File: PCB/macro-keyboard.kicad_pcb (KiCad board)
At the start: 2 copper layers, 77.6 x 43 mm, 38 parts, among them SW1 SW_Push, SW2 SW_Push, SW3 SW_Push, SW4 SW_Push, SW5 SW_Push, SW6 SW_Push, SW7 SW_Push, SW8 SW_Push, U1 PRTR5V0U2X, U2 ATmega32U4-A, Y1 Crystal_GND24_Small

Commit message: Add gerber files
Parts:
- moved REF** 0.08 mm to (165.9, 83.3)
- moved REF** 0.08 mm to (126.9, 83.4)
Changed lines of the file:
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@@
 			(disableapertmacros no)
 			(usegerberextensions no)
-			(usegerberattributes yes)
-			(usegerberadvancedattributes yes)
-			(creategerberjobfile yes)
+			(usegerberattributes no)
+			(usegerberadvancedattributes no)
+			(creategerberjobfile no)
 			(dashed_line_dash_ratio 12.000000)
 			(dashed_line_gap_ratio 3.000000)
 			(svgprecision 4)
 			(plotframeref no)
-			(viasonmask no)
+			(viasonmask yes)
 			(mode 1)
 			(useauxorigin no)
@@
 			(outputformat 1)
 			(mirror no)
-			(drillshape 1)
+			(drillshape 0)
 			(scaleselection 1)
-			(outputdirectory "")
+			(outputdirectory "Fabrication/")
 		)
 	)
@@
 	(footprint "MountingHole:MountingHole_2.2mm_M2_DIN965"
 		(layer "F.Cu")
-		(at 146.4 109)
+		(at 146.425 108.975)
 		(descr "Mounting Hole 2.2mm, no annular, M2, DIN965")
 		(tags "mounting hole 2.2mm no annular m2 din965")
@@
 	(footprint "MountingHole:MountingHole_2.2mm_M2_DIN965"
 		(layer "F.Cu")
-		(at 165.9 83.4)
+		(at 165.925 83.325)
 		(descr "Mounting Hole 2.2mm, no annular, M2, DIN965")
 		(tags "mounting hole 2.2mm no annular m2 din965")
@@
 	(footprint "MountingHole:MountingHole_2.2mm_M2_DIN965"
 		(layer "F.Cu")
-		(at 126.9 83.3)
+		(at 126.925 83.375)
 		(descr "Mounting Hole 2.2mm, no annular, M2, DIN965")
 		(tags "mounting hole 2.2mm no annular m2 din965")
@@
 	)
 	(segment
+		(start 175.4 95.8)
+		(end 177.2 97.6)
+		(width 0.381)
+		(layer "B.Cu")
+		(net 2)
+	)
+	(segment
 		(start 175.724264 94.024264)
 		(end 176.123044 94.024264)
@@
 	)
 	(segment
-		(start 175.4 95.8)
-		(end 177.319 97.719)
+		(start 179.580062 97.6)
+		(end 179.689421 97.490641)
 		(width 0.381)
 		(layer "B.Cu")
@@
 	)
 	(segment
-		(start 179.461062 97.719)
-		(end 179.689421 97.490641)
+		(start 177.2 97.6)
+		(end 179.580062 97.6)
 		(width 0.381)
 		(layer "B.Cu")
@@
 	)
 	(segment
-		(start 177.319 97.719)
-		(end 179.461062 97.719)
-		(width 0.381)
-		(layer "B.Cu")
-		(net 2)
-	)
-	(segment
 		(start 175.4 94.747308)
 		(end 175.4 95.8)
@@
 	)
 	(segment
-		(start 166.029169 103.177275)
-		(end 165.515454 103.177275)
-		(width 0.381)
-		(layer "B.Cu")
-		(net 4)
-	)
-	(segment
 		(start 142.166377 86.533623)
 		(end 142.433623 86.533623)
@@
 	)
 	(segment
-		(start 166.885786 108.614214)
-		(end 166.820421 108.548849)
-		(width 0.381)
-		(layer "B.Cu")
-		(net 4)
-	)
-	(segment
 		(start 142.113623 79.786377)
 		(end 142.113623 80.463623)
@@
 	)
 	(segment
+		(start 166.820421 103.569474)
+		(end 166.175947 102.925)
+		(width 0.381)
+		(layer "B.Cu")
+		(net 4)
+	)
+	(segment
 		(start 181.156667 97.259107)
 		(end 181.156667 98.957887)
@@
 	)
 	(segment
+		(start 166.175947 99.875947)
+		(end 166.175947 102.925)
+		(width 0.381)
+		(layer "B.Cu")
+		(net 4)
+	)
+	(segment
 		(start 178.030642 92.116666)
 		(end 178.030642 95.369358)
@@
 	)
 	(segment
+		(start 166.820421 108.548849)
+		(end 166.820421 103.569474)
+		(width 0.381)
+		(layer "B.Cu")
+		(net 4)
+	)
+	(segment
 		(start 162.137429 93.9688)
 		(end 160.767246 92.598617)
@@
 	)
 	(segment
-		(start 165.515454 103.177275)
-		(end 164.965856 103.726873)
+		(start 183.156667 96.957887)
+		(end 181.157887 96.957887)
 		(width 0.381)
 		(layer "B.Cu")
@@
 	)
 	(segment
-		(start 166.820421 103.968527)
-		(end 166.175947 103.324053)
+		(start 150.753623 79.753623)
+		(end 149.7 78.7)
 		(width 0.381)
 		(layer "B.Cu")
@@
 	)
 	(segment
-		(start 183.156667 96.957887)
-		(end 181.157887 96.957887)
+		(start 163.166377 105.533623)
+		(end 163.166377 105.666377)
 		(width 0.381)
 		(layer "B.Cu")
@@
 	)
 	(segment
-		(start 150.753623 79.753623)
-		(end 149.7 78.7)
+		(start 171.627736 96.670882)
+		(end 173.592559 98.635705)
 		(width 0.381)
 		(layer "B.Cu")
@@
 	)
 	(segment
-		(start 163.166377 105.533623)
-		(end 163.166377 105.666377)
+		(start 166.175947 102.925)
+		(end 165.767729 102.925)
 		(width 0.381)
 		(layer "B.Cu")
@@
 	)
 	(segment
-		(start 171.627736 96.670882)
-		(end 173.592559 98.635705)
+		(start 162.970882 96.670882)
+		(end 166.175947 99.875947)
 		(width 0.381)
 		(layer "B.Cu")
@@
 	)
 	(segment
+		(start 166.885786 108.614214)
+		(end 166.820421 108.548849)
+		(width 0.381)
+		(layer "B.Cu")
+		(net 4)
+	)
+	(segment
 		(start 140.448123 88.251877)
 		(end 142.166377 86.533623)
@@
 	)
 	(segment
-		(start 166.175947 103.324053)
-		(end 166.175947 99.875947)
+		(start 157.350989 99.750989)
+		(end 156.867246 99.267246)
 		(width 0.381)
 		(layer "B.Cu")
@@
 	)
 	(segment
-		(start 157.350989 99.750989)
-		(end 156.867246 99.267246)
+		(start 165.767729 102.925)
+		(end 164.965856 103.726873)
 		(width 0.381)
 		(layer "B.Cu")
@@
 	)
 	(segment
-		(start 166.820421 108.548849)
-		(end 166.820421 103.968527)
-		(width 0.381)
-		(layer "B.Cu")
-		(net 4)
-	)
-	(segment
 		(start 179.4 99.5)
 		(end 180.614554 99.5)
@@
 	)
 	(segment
-		(start 166.175947 103.324053)
-		(end 166.029169 103.177275)
-		(width 0.381)
-		(layer "B.Cu")
-		(net 4)
-	)
-	(segment
 		(start 150.753623 80.463623)
 		(end 150.753623 76.283623)
@@
 		(width 0.381)
 		(layer "B.Cu")
-		(net 4)
-	)
-	(segment
-		(start 166.175947 99.875947)
-		(end 162.970882 96.670882)
-		(width 0.381)
-		(layer "B.Cu")

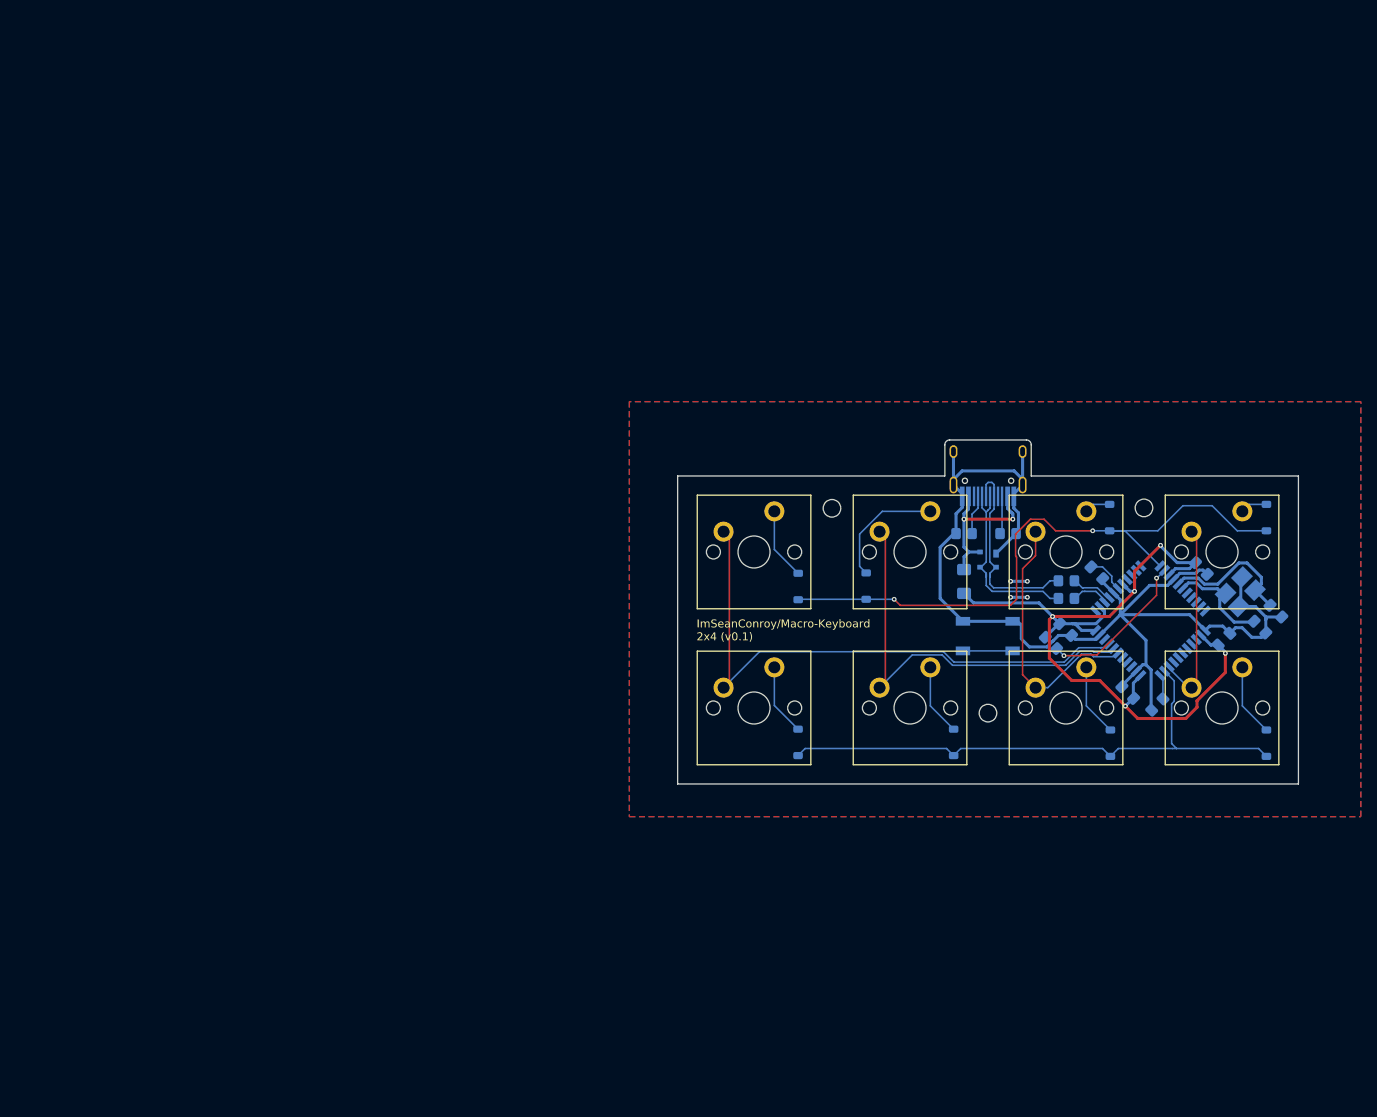
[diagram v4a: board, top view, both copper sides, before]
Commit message: Add boxes to schematic
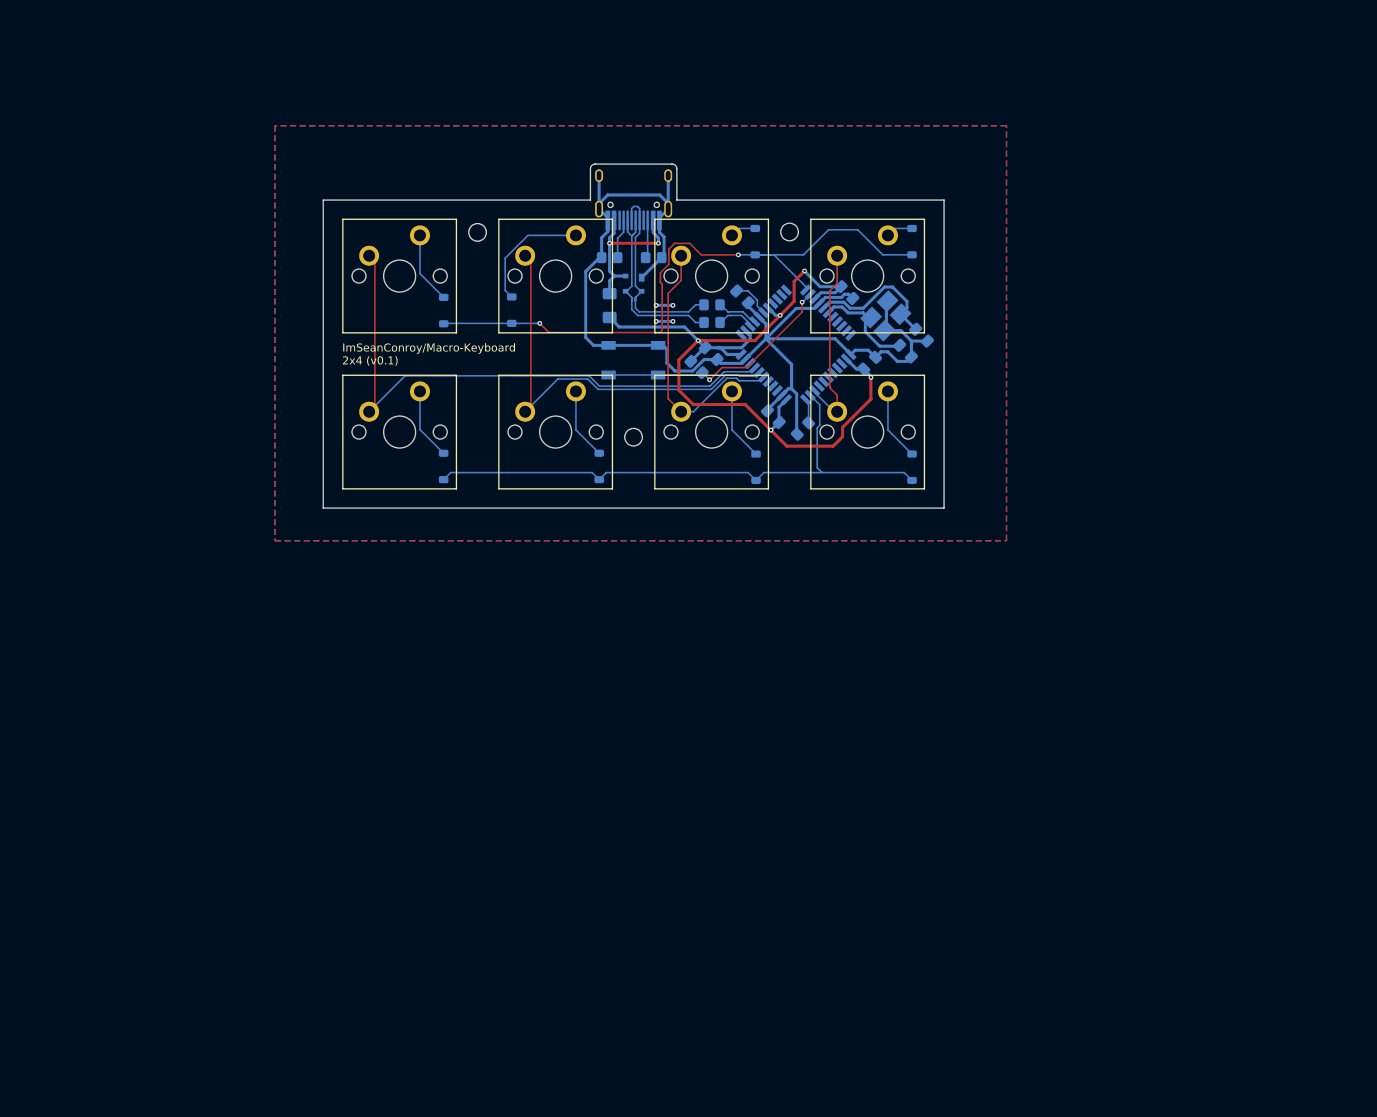
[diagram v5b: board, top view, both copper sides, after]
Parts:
- moved C1 56.1 mm to (136.1, 63.7)
- moved C2 56.1 mm to (138.1, 61.7)
- moved C3 56.1 mm to (131.6, 65.2)
- moved C5 56.1 mm to (119.6, 71.9)
- moved C8 56.1 mm to (115.7, 56.9)
- moved F1 56.1 mm to (99.1, 58.0)
- moved R1 56.1 mm to (104.6, 52.0)
- moved R2 56.1 mm to (99.1, 52.0)
- moved R5 56.1 mm to (110.0, 65.7)
- moved REF** 56.1 mm to (102.1, 74.5)
- moved REF** 56.1 mm to (121.6, 48.8)
- moved SW13 56.1 mm to (102.1, 64.9)
- moved SW2 56.1 mm to (92.4, 54.3)
- moved SW3 56.1 mm to (111.9, 54.3)
- moved SW4 56.1 mm to (131.4, 54.3)
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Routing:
- net +5V: track 100.9 -> 104.9 mm
- net col3: track 24.0 -> 26.1 mm
- net row0: track 79.6 -> 80.9 mm
- net GND: track 147.0 -> 148.0 mm
- net RESET: track 31.4 -> 30.8 mm

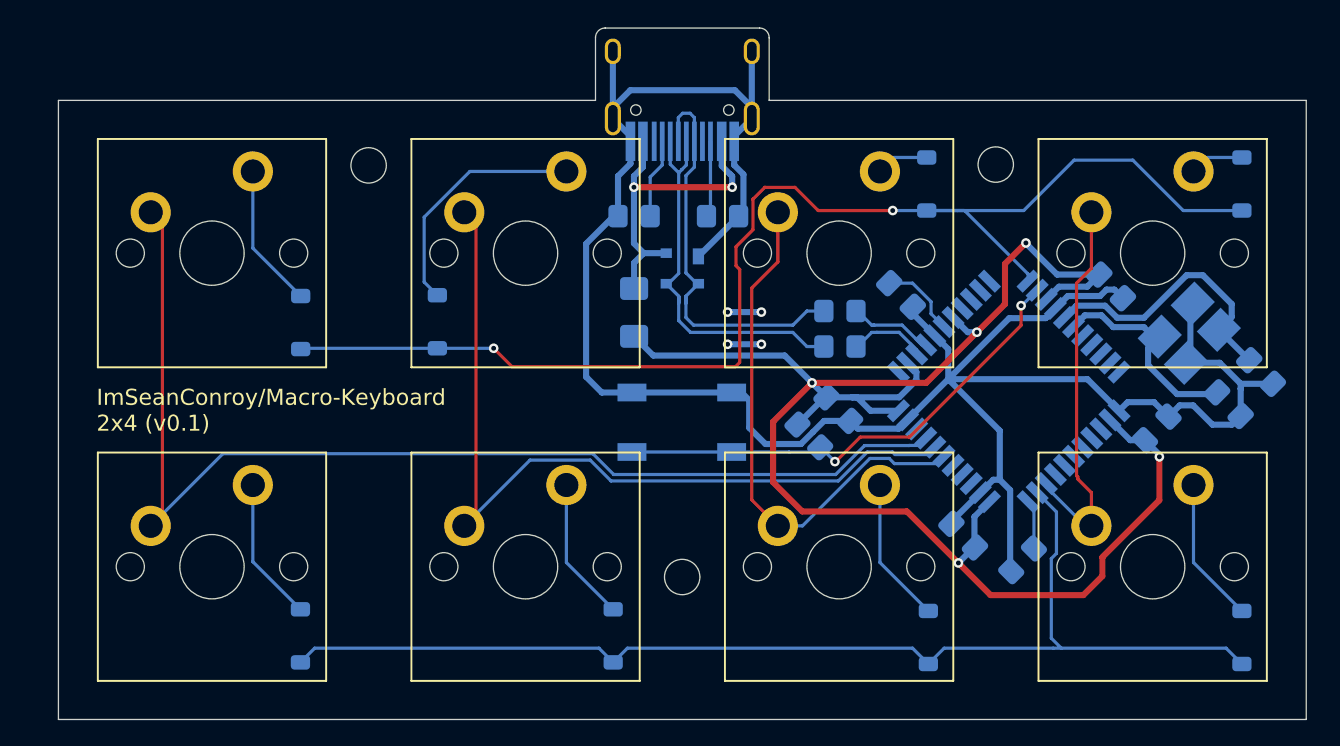
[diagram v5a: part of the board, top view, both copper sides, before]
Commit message: Add missing decoupling capacitor
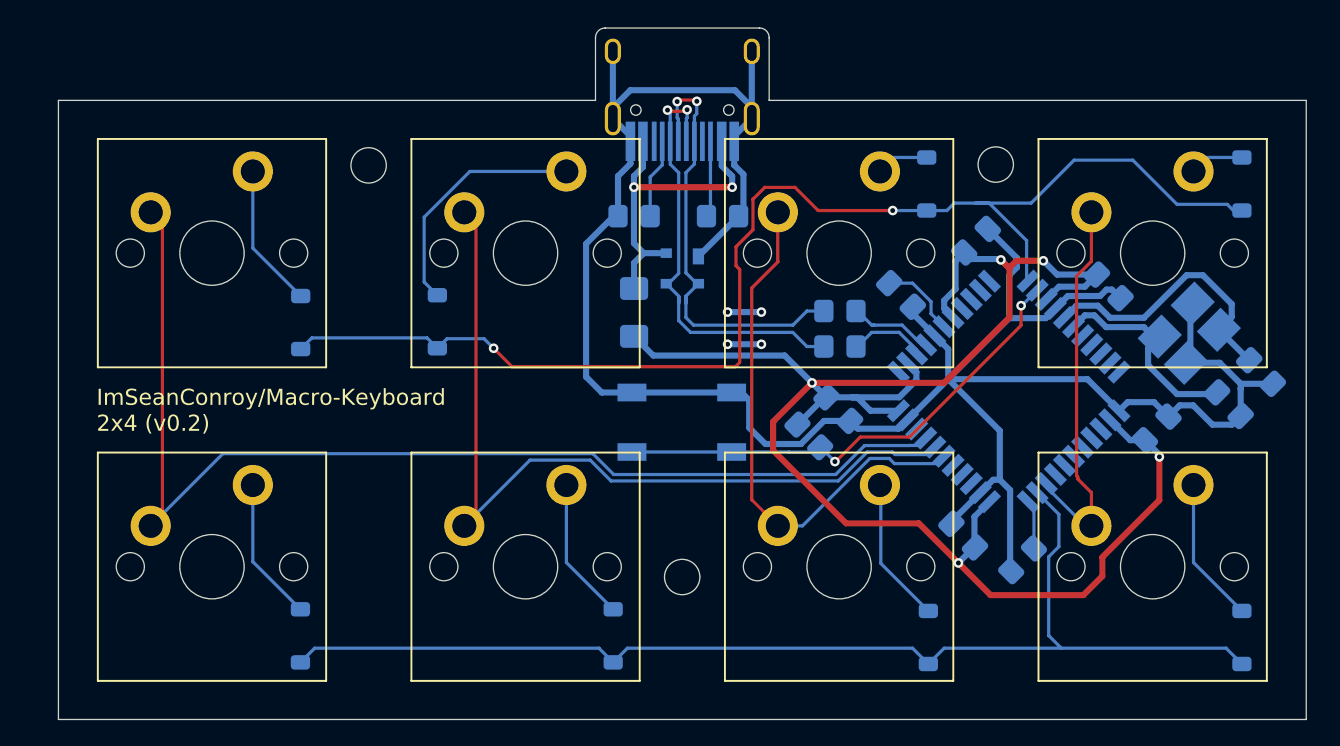
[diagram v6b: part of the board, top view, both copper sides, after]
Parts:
- added C6: 0.1u, Capacitor_SMD:C_0805_2012Metric_Pad1.18x1.45mm_HandSolder, B.Cu at (120.4, 53.6)
- C8: value C_Small -> 1u
- R6: value R_Small -> 10k
- moved C4 0.15 mm to (128.7, 56.4)
- renumbered REF** to HOLE1, REF** to HOLE2, REF** to HOLE3
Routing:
- net GND: track 148.0 -> 154.4 mm
- net +5V: track 104.9 -> 109.0 mm
- net DN: track 24.8 -> 27.9 mm, vias 0 -> 2
- net DP: track 26.0 -> 28.3 mm, vias 0 -> 2
- net col3: track 26.1 -> 24.3 mm
- net row0: track 80.9 -> 80.2 mm
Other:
- board text added: "ImSeanConroy/Macro-Keyboard 2x4 (v0.2)"
- board text removed: "ImSeanConroy/Macro-Keyboard 2x4 (v0.1)"

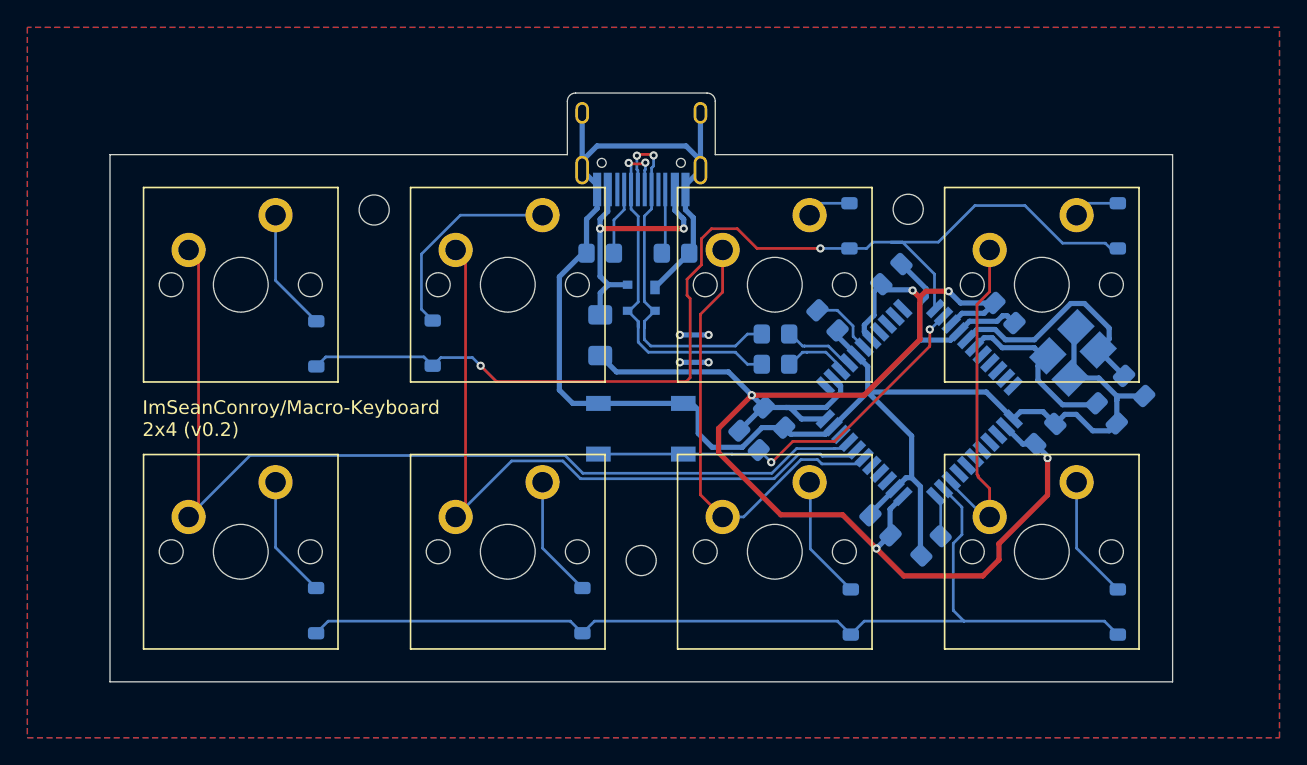
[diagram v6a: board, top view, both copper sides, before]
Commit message: Convert to 4 layer board and update traces
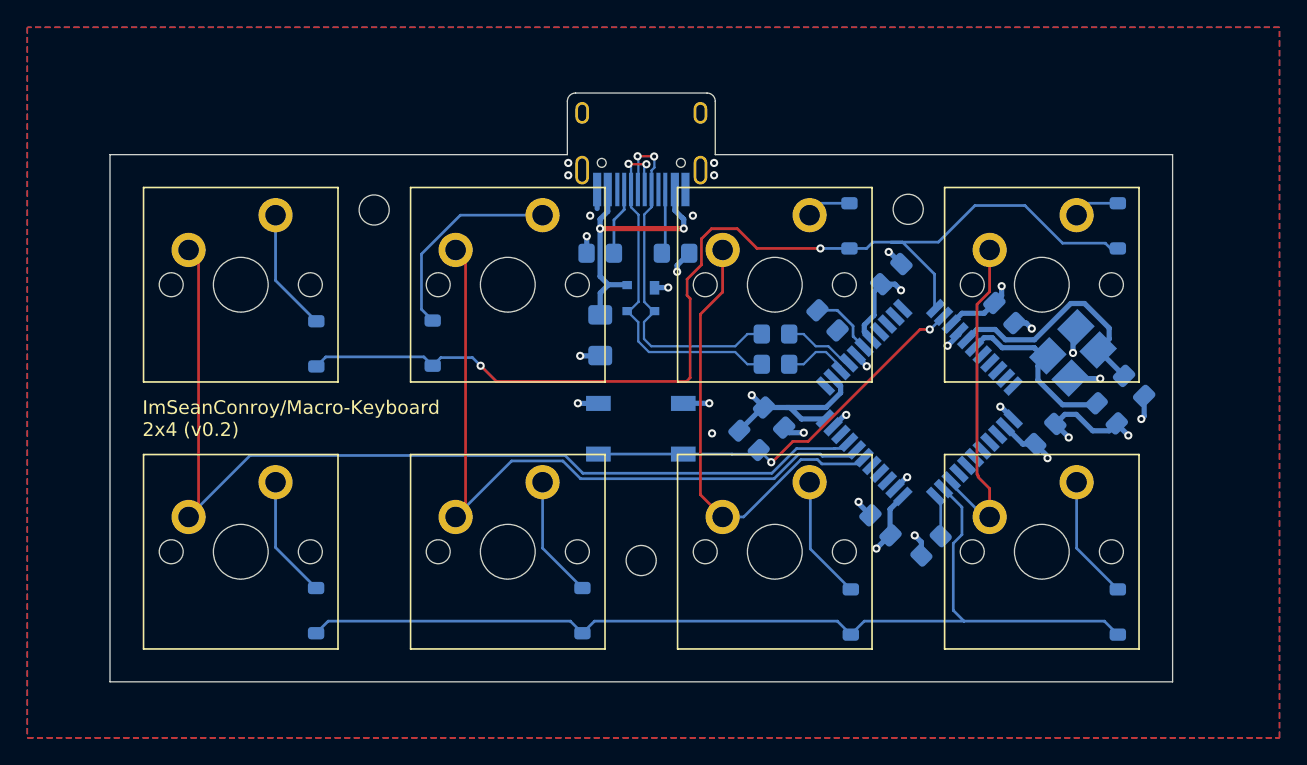
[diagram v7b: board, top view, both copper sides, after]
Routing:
- net GND: track 154.4 -> 40.4 mm, vias 4 -> 26
- net +5V: track 109.0 -> 113.1 mm, vias 5 -> 7
- net RESET: track 30.8 -> 30.1 mm
- added copper zone on In1.Cu, net GND
- added copper zone on In2.Cu, net GND
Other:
- copper layers 2 -> 4
